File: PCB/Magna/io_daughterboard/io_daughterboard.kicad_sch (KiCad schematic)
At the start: 15 parts, among them J101 Conn_02x10_Counter_Clockwise, U101 NE5532, U102 NE5532, U103 NE5532

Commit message: Route most of io daughterboard
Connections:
- net ADC_0_CONN: now also J101.7 (Pin_7); no longer J101.8 (Pin_8)
- net ADC_1_CONN: now also J101.5 (Pin_5); no longer J101.6 (Pin_6)
- net ADC_2_CONN: now also J101.3 (Pin_3); no longer J101.4 (Pin_4)
- net ADC_3_CONN: now also J101.1 (Pin_1); no longer J101.2 (Pin_2)
- net ADC_4_CONN: now also J101.4 (Pin_4); no longer J101.3 (Pin_3)
- net ADC_5_CONN: now also J101.6 (Pin_6); no longer J101.5 (Pin_5)
- net Buttons/I2C_SCL: now also J101.16 (Pin_16); no longer J101.19 (Pin_19)
- net Buttons/I2C_SDA: now also J101.20 (Pin_20); no longer J101.15 (Pin_15)
- net Buttons/button_interrupt: now also J101.8 (Pin_8); no longer J101.7 (Pin_7)
- net GND: now also J101.12 (Pin_12), J101.18 (Pin_18), U101.8 (V+), U102.8 (V+), U103.8 (V+); no longer J101.11 (Pin_11), J101.17 (Pin_17), U101.4 (V-), U102.4 (V-), U103.4 (V-)
- net VDD: now also J101.19 (Pin_19); no longer J101.20 (Pin_20)
- net VDDA: now also J101.2 (Pin_2), U101.4 (V-), U102.4 (V-), U103.4 (V-); no longer J101.1 (Pin_1), U101.8 (V+), U102.8 (V+), U103.8 (V+)
- net lsb: now also J101.14 (Pin_14); no longer J101.13 (Pin_13)
- net msb: now also J101.10 (Pin_10); no longer J101.9 (Pin_9)
- net register_CLK: now also J101.13 (Pin_13); no longer J101.16 (Pin_16)
- net register_OE: now also J101.9 (Pin_9); no longer J101.10 (Pin_10)
- net serial_CLK: now also J101.17 (Pin_17); no longer J101.12 (Pin_12)
- net serial_CLR: now also J101.15 (Pin_15); no longer J101.14 (Pin_14)
- net serial_data: now also J101.11 (Pin_11); no longer J101.18 (Pin_18)
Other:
- moved on the sheet: U101C, U102C, U103C

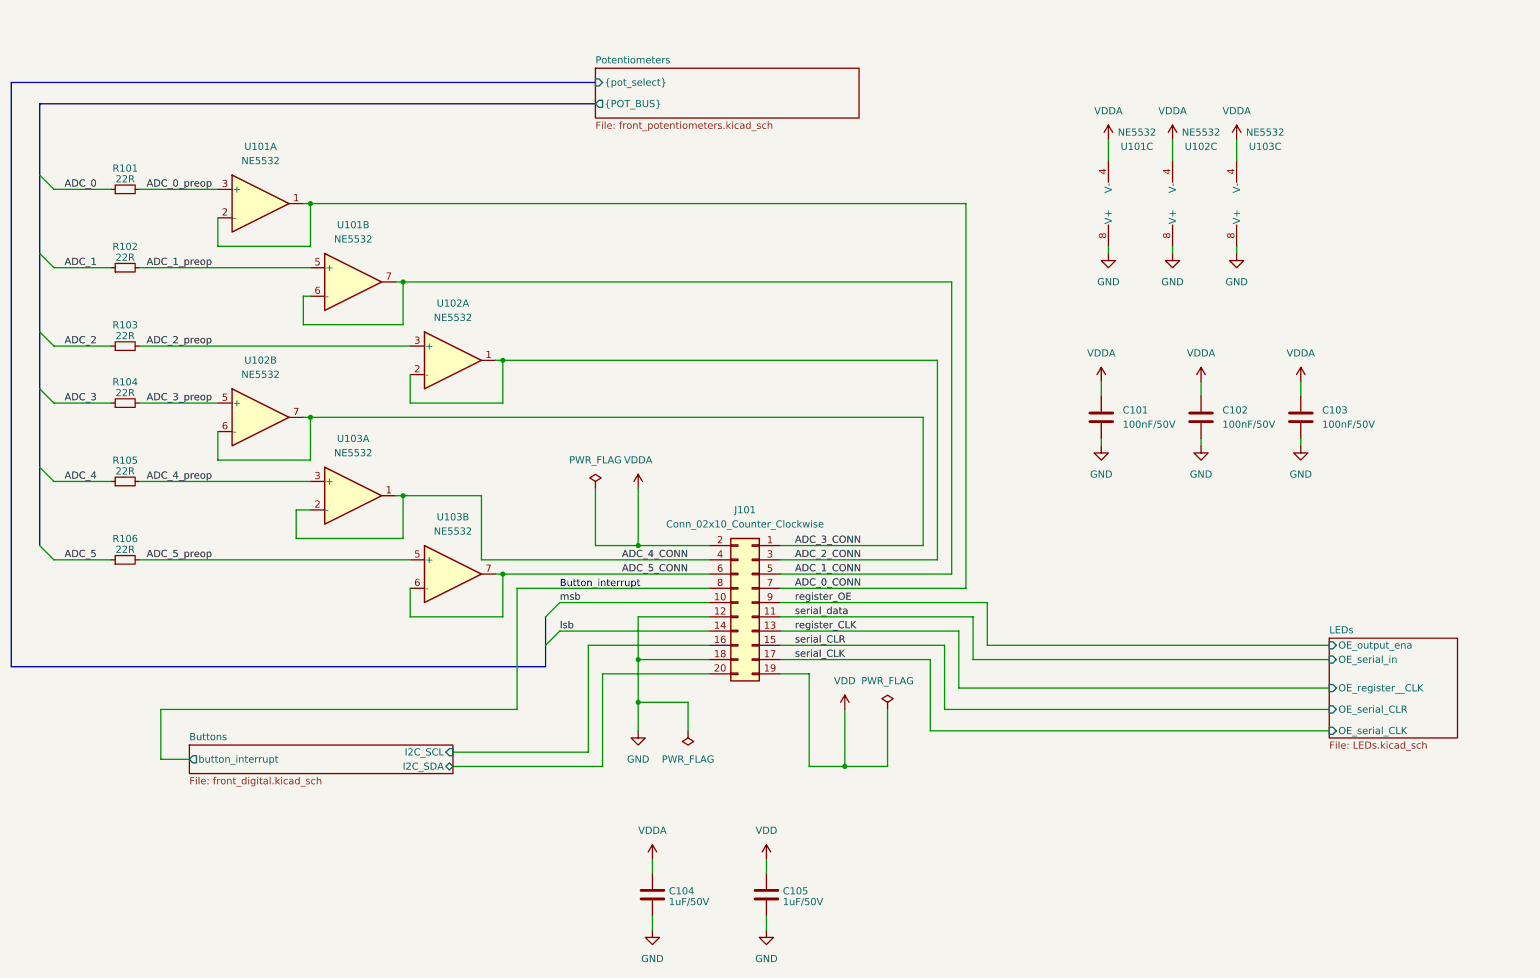
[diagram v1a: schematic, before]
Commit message: Add more routing to IO Daugherboard
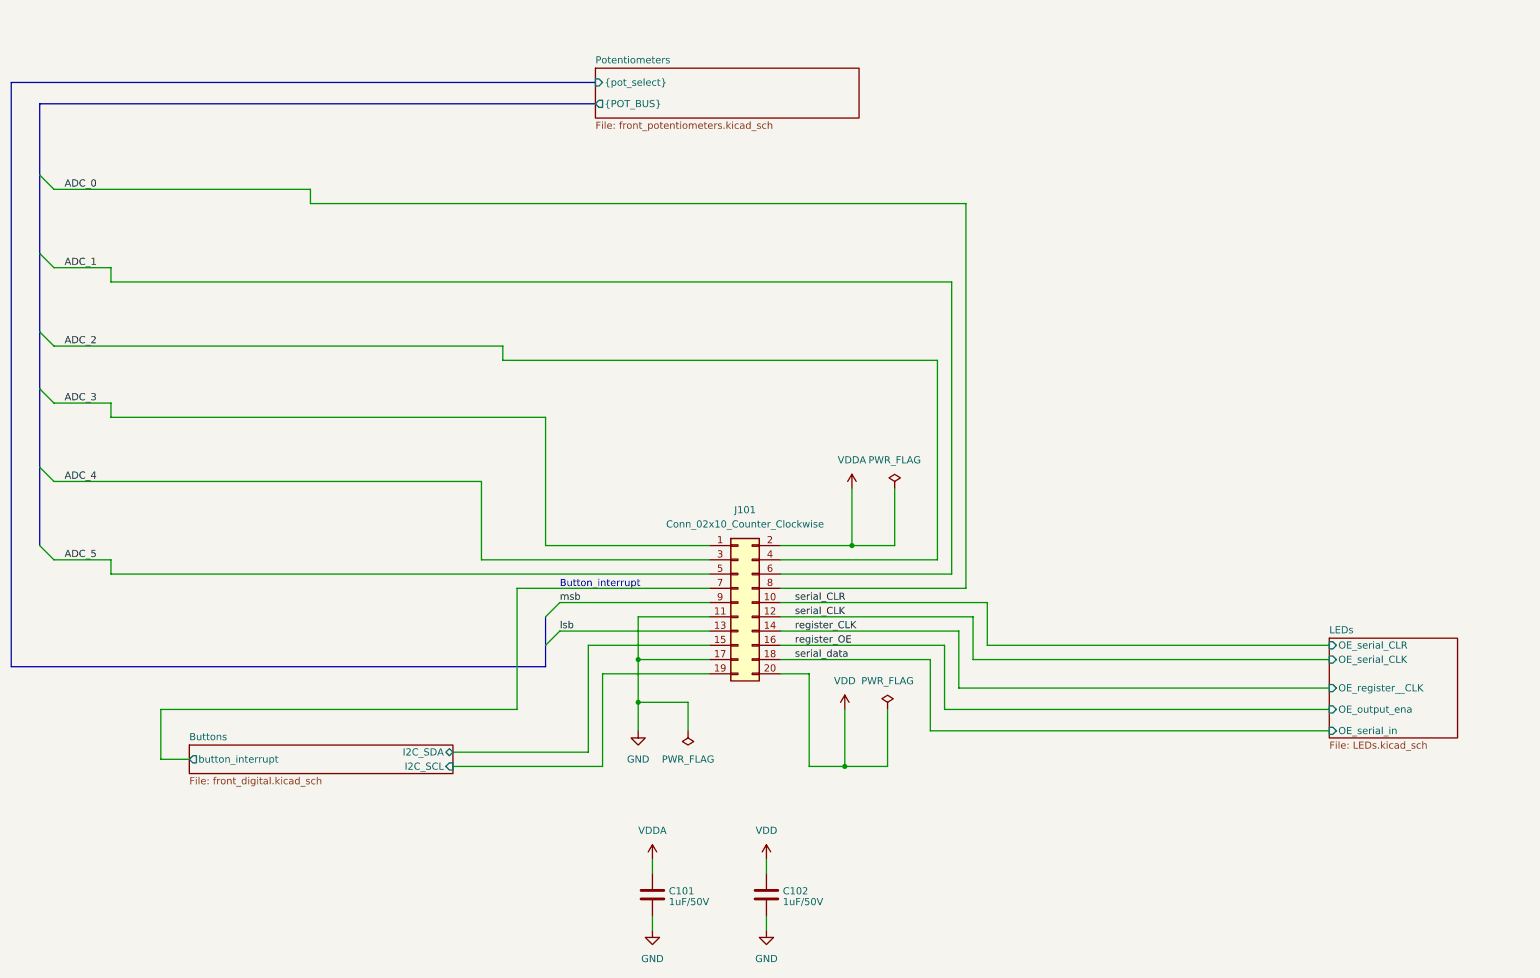
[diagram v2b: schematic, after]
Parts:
- removed C101, C102, C103: 100nF/50V, Capacitor_SMD:C_0805_2012Metric_Pad1.18x1.45mm_HandSolder, symbol Device:C
- removed R101, R102, R103, R104, R105, R106: 22R, Resistor_SMD:R_0805_2012Metric_Pad1.20x1.40mm_HandSolder, symbol Device:R_Small
- removed U101, U102, U103: NE5532, Package_SO:SOIC-8_3.9x4.9mm_P1.27mm, symbol Amplifier_Operational:NE5532
- renumbered C104 to C101, C105 to C102
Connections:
- net ADC_0_CONN is gone; now on net Buttons/button_interrupt: J101.7 (Pin_7)
- net ADC_1_CONN is gone; now on net ADC_5: J101.5 (Pin_5)
- net ADC_2_CONN is gone; now on net ADC_4: J101.3 (Pin_3)
- net ADC_3_CONN is gone; now on net ADC_3: J101.1 (Pin_1)
- net ADC_4_CONN is gone; now on net ADC_2: J101.4 (Pin_4)
- net ADC_5_CONN is gone; now on net ADC_1: J101.6 (Pin_6)
- net ADC_0: now also J101.8 (Pin_8)
- net Buttons/I2C_SCL: now also J101.19 (Pin_19); no longer J101.16 (Pin_16)
- net Buttons/I2C_SDA: now also J101.15 (Pin_15); no longer J101.20 (Pin_20)
- net Buttons/button_interrupt: no longer J101.8 (Pin_8)
- net GND: now also J101.11 (Pin_11), J101.17 (Pin_17); no longer J101.12 (Pin_12), J101.18 (Pin_18)
- net VDD: now also J101.20 (Pin_20); no longer J101.19 (Pin_19)
- net lsb: now also J101.13 (Pin_13); no longer J101.14 (Pin_14)
- net msb: now also J101.9 (Pin_9); no longer J101.10 (Pin_10)
- net register_CLK: now also J101.14 (Pin_14); no longer J101.13 (Pin_13)
- net register_OE: now also J101.16 (Pin_16); no longer J101.9 (Pin_9)
- net serial_CLK: now also J101.12 (Pin_12); no longer J101.17 (Pin_17)
- net serial_CLR: now also J101.10 (Pin_10); no longer J101.15 (Pin_15)
- net serial_data: now also J101.18 (Pin_18); no longer J101.11 (Pin_11)

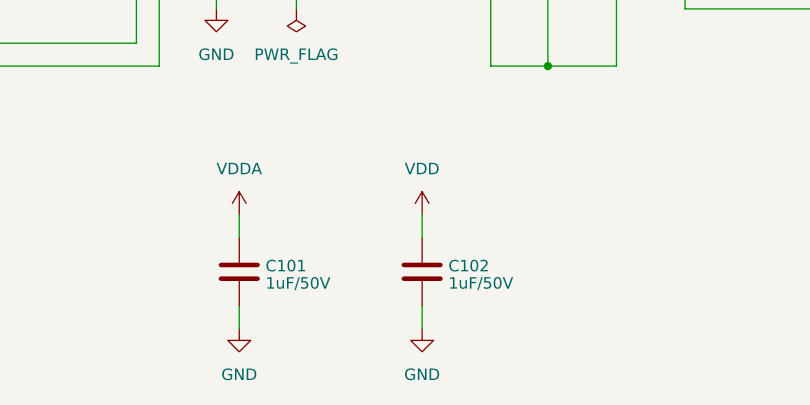
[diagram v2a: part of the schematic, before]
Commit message: Change all capacitors to 22uF on IO board(#5)
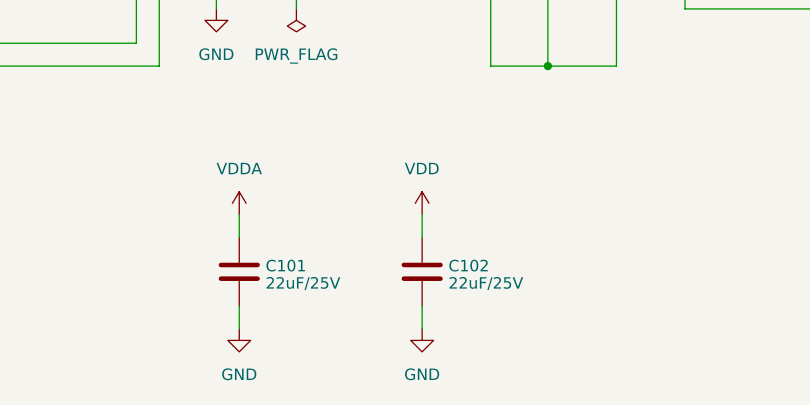
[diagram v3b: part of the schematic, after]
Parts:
- C101, C102: value 1uF/50V -> 22uF/25V; LCSC C28323 -> C45783
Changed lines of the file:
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@@
       (effects (font (size 1.27 1.27)) (justify left))
     )
-    (property "Value" "1uF/50V" (at 131.191 171.4573 0)
+    (property "Value" "22uF/25V" (at 131.191 171.4573 0)
       (effects (font (size 1.27 1.27)) (justify left))
     )
@@
       (effects (font (size 1.27 1.27)) hide)
     )
-    (property "LCSC" "C28323" (at 128.27 170.18 0)
+    (property "LCSC" "C45783" (at 128.27 170.18 0)
       (effects (font (size 1.27 1.27)) hide)
     )
@@
       (effects (font (size 1.27 1.27)) (justify left))
     )
-    (property "Value" "1uF/50V" (at 151.511 171.4573 0)
+    (property "Value" "22uF/25V" (at 151.511 171.4573 0)
       (effects (font (size 1.27 1.27)) (justify left))
     )
@@
       (effects (font (size 1.27 1.27)) hide)
     )
-    (property "LCSC" "C28323" (at 148.59 170.18 0)
+    (property "LCSC" "C45783" (at 148.59 170.18 0)
       (effects (font (size 1.27 1.27)) hide)
     )
